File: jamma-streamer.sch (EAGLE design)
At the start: 63 parts, among them IC1 LM7805, J1 Audio line out, J2 ICSP, J3 SDCARD, J4 USB, T1 TY-145P, T2 TY-145P, U1 CD74HC165MD16-M, U10 LM358DTD8-M, U2 ATMEGA328PB-AUR, U3 74HC4050D, U4 TLV757X / LP298X, U5 CD74HC165MD16-M, U6 CD74HC165MD16-M, U7 FT232RL, U8 DS3231SNT&R21-0042B_16-M, U9 NDT2955SOT-223-M, Y1 16MHz

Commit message: Better routing, elec fixes, doc and sdcard ok
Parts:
- added C14: 0.1uF/16V, CMS:KEMET-C1210C104K4J
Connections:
- net GND: now also C14.P$2, J3.DAT1, J3.DAT2
- net VCC: now also C14.P$1
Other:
- note added: "After tests: - DAT1 and DAT2 could be floating or GND - DI = MOSI = CMD - DO = MISO - SCK = CLOCK SD Status is working and inspired from the following: https://learn.adafruit.com/adafruit-micro-sd-breakout-board-card-tutorial?view=all"
- note added: "CS = PB2 (atmega) = Pin 10 (arduino pin number) Used by "ArduinoISP sketch" to send a reset signal when using this ATmega as ISP programmer."
- note removed: "CS = PB2 = Pin 10 Used by ArduinoISP sketch to send a reset signal when using this atmega as ISP programmer"
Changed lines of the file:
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@@
 <part name="GND33" library="SparkFun-PowerSymbols" library_urn="urn:adsk.eagle:library:530" deviceset="GND" device=""/>
 <part name="SUPPLY22" library="SparkFun-PowerSymbols" library_urn="urn:adsk.eagle:library:530" deviceset="VCC" device=""/>
-<part name="SUPPLY23" library="SparkFun-PowerSymbols" library_urn="urn:adsk.eagle:library:530" deviceset="VCCIO" device=""/>
+<part name="C14" library="CMS" deviceset="KEMET-C1210C104K4J" device="" value="0.1uF/16V"/>
+<part name="GND34" library="SparkFun-PowerSymbols" library_urn="urn:adsk.eagle:library:530" deviceset="GND" device=""/>
+<part name="SUPPLY16" library="SparkFun-PowerSymbols" library_urn="urn:adsk.eagle:library:530" deviceset="VCC" device=""/>
 </parts>
 <sheets>
@@
 </segment>
 </net>
-<net name="USBVCC" class="0">
-<segment>
-<pinref part="U9" gate="A" pin="D"/>
-<wire x1="101.6" y1="109.22" x2="109.22" y2="109.22" width="0.1524" layer="91"/>
-<label x="109.22" y="109.22" size="1.27" layer="95" xref="yes"/>
-</segment>
-</net>
 <net name="N$23" class="0">
 <segment>
@@
 </segment>
 </net>
+<net name="USBVCC" class="0">
+<segment>
+<pinref part="U9" gate="A" pin="D"/>
+<wire x1="101.6" y1="109.22" x2="111.76" y2="109.22" width="0.1524" layer="91"/>
+<label x="111.76" y="109.22" size="1.27" layer="95" xref="yes"/>
+</segment>
+</net>
 </nets>
 </sheet>
@@
 <description>Micro SD CARD related circuitry</description>
 <plain>
+<text x="-5.08" y="50.8" size="1.27" layer="91" font="fixed">After tests:
+  - DAT1 and DAT2 could be floating or GND
+  - DI  = MOSI = CMD
+  - DO  = MISO
+  - SCK = CLOCK
+SD Status is working and inspired from the following:
+https://learn.adafruit.com/adafruit-micro-sd-breakout-board-card-tutorial?view=all</text>
 </plain>
 <instances>
@@
 <wire x1="96.52" y1="10.16" x2="96.52" y2="7.62" width="0.1524" layer="91"/>
 <junction x="96.52" y="7.62"/>
+<pinref part="J3" gate="G$1" pin="DAT2"/>
+<wire x1="101.6" y1="17.78" x2="96.52" y2="17.78" width="0.1524" layer="91"/>
+<wire x1="96.52" y1="17.78" x2="96.52" y2="10.16" width="0.1524" layer="91"/>
+<junction x="96.52" y="10.16"/>
+<pinref part="J3" gate="G$1" pin="DAT1"/>
+<wire x1="101.6" y1="20.32" x2="96.52" y2="20.32" width="0.1524" layer="91"/>
+<wire x1="96.52" y1="20.32" x2="96.52" y2="17.78" width="0.1524" layer="91"/>
+<junction x="96.52" y="17.78"/>
 </segment>
 <segment>
@@
 <attribute name="VALUE" x="111.76" y="109.474" size="1.778" layer="96" align="bottom-center"/>
 </instance>
-<instance part="GND6" gate="1" x="111.76" y="45.72" smashed="yes">
-<attribute name="VALUE" x="111.76" y="45.466" size="1.778" layer="96" align="top-center"/>
+<instance part="GND6" gate="1" x="111.76" y="50.8" smashed="yes" rot="R90">
+<attribute name="VALUE" x="112.014" y="50.8" size="1.778" layer="96" rot="R90" align="top-center"/>
 </instance>
 <instance part="R2" gate="A" x="45.72" y="50.8" smashed="yes">
@@
 <instance part="GND15" gate="1" x="27.94" y="93.98" smashed="yes">
 <attribute name="VALUE" x="27.94" y="93.726" size="1.778" layer="96" align="top-center"/>
+</instance>
+<instance part="C14" gate="A" x="119.38" y="101.6" smashed="yes" rot="R90">
+<attribute name="NAME" x="117.88" y="98.6" size="1.27" layer="94" rot="R90"/>
+<attribute name="VALUE" x="122.38" y="98.6" size="1.27" layer="94" rot="R90"/>
+</instance>
+<instance part="GND34" gate="1" x="119.38" y="93.98" smashed="yes">
+<attribute name="VALUE" x="119.38" y="93.726" size="1.778" layer="96" align="top-center"/>
+</instance>
+<instance part="SUPPLY16" gate="G$1" x="119.38" y="106.68" smashed="yes">
+<attribute name="VALUE" x="119.38" y="109.474" size="1.778" layer="96" align="bottom-center"/>
 </instance>
 </instances>
@@
 <segment>
 <pinref part="U2" gate="G$1" pin="GND"/>
-<wire x1="91.44" y1="50.8" x2="111.76" y2="50.8" width="0.1524" layer="91"/>
+<wire x1="91.44" y1="50.8" x2="109.22" y2="50.8" width="0.1524" layer="91"/>
 <pinref part="GND6" gate="1" pin="GND"/>
-<wire x1="111.76" y1="50.8" x2="111.76" y2="48.26" width="0.1524" layer="91"/>
 </segment>
 <segment>
@@
 <wire x1="27.94" y1="97.79" x2="24.13" y2="97.79" width="0.1524" layer="91"/>
 </segment>
+<segment>
+<pinref part="C14" gate="A" pin="P$2"/>
+<wire x1="119.38" y1="98.608" x2="119.38" y2="96.52" width="0.1524" layer="91"/>
+<pinref part="GND34" gate="1" pin="GND"/>
+</segment>
 </net>
 <net name="VCC" class="0">
@@
 <wire x1="24.13" y1="102.87" x2="26.67" y2="102.87" width="0.1524" layer="91"/>
 <label x="26.67" y="102.87" size="1.27" layer="95" font="vector" xref="yes"/>
+</segment>
+<segment>
+<pinref part="C14" gate="A" pin="P$1"/>
+<wire x1="119.38" y1="104.592" x2="119.38" y2="106.68" width="0.1524" layer="91"/>
+<pinref part="SUPPLY16" gate="G$1" pin="VCC"/>
 </segment>
 </net>
@@
 <description>USB input</description>
 <plain>
-<text x="104.14" y="73.66" size="1.778" layer="91">CS = PB2 = Pin 10
-Used by ArduinoISP sketch to send a reset
-signal when using this atmega as ISP programmer</text>
+<text x="104.14" y="73.66" size="1.778" layer="91">CS = PB2 (atmega) = Pin 10 (arduino pin number)
+Used by "ArduinoISP sketch" to send a reset
+signal when using this ATmega as ISP programmer.</text>
 </plain>
 <instances>
@@
 <attribute name="NAME" x="124.46" y="53.34" size="1.778" layer="95"/>
 <attribute name="VALUE" x="124.46" y="46.99" size="1.778" layer="96"/>
-</instance>
-<instance part="SUPPLY23" gate="G$1" x="15.24" y="12.7" smashed="yes" rot="R90">
-<attribute name="VALUE" x="12.446" y="12.7" size="1.778" layer="96" rot="R90" align="bottom-center"/>
 </instance>
 </instances>
@@
 <wire x1="66.04" y1="55.88" x2="66.04" y2="50.8" width="0.1524" layer="91"/>
 <wire x1="66.04" y1="50.8" x2="43.18" y2="50.8" width="0.1524" layer="91"/>
-<wire x1="43.18" y1="50.8" x2="43.18" y2="66.04" width="0.1524" layer="91"/>
 <junction x="43.18" y="50.8"/>
-<label x="43.18" y="66.04" size="1.27" layer="95" rot="R90" xref="yes"/>
+<label x="43.18" y="73.66" size="1.27" layer="95" rot="R90" xref="yes"/>
 <wire x1="68.58" y1="48.26" x2="43.18" y2="48.26" width="0.1524" layer="91"/>
 <junction x="43.18" y="48.26"/>
-</segment>
-<segment>
+<wire x1="43.18" y1="50.8" x2="43.18" y2="73.66" width="0.1524" layer="91"/>
+<wire x1="43.18" y1="72.12" x2="43.18" y2="50.8" width="0.1524" layer="91"/>
+</segment>
+<segment>

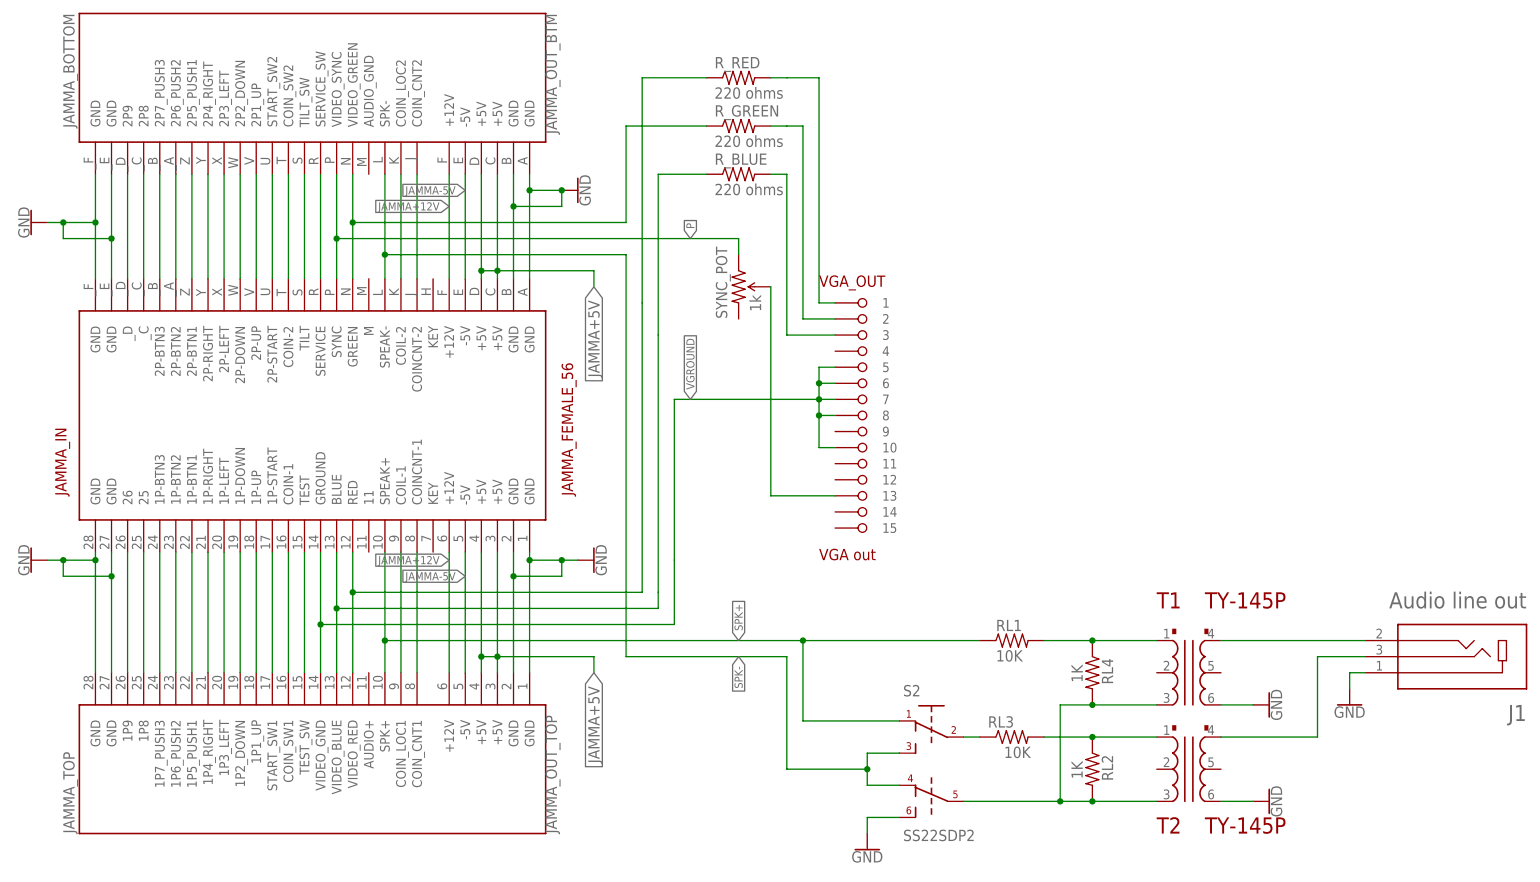
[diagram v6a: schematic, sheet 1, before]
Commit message: Refacto some parts on the PCB
- new SDCARD slot (push-push): https://www.mouser.fr/ProductDetail/798-DM3AT-SF-PEJM5
- new microUSB connector (type B): https://www.mouser.fr/ProductDetail/806-KMMXBSMT35SB30TR
- resistors replacement for audio (3W) -> need to replace with other
values
- resistors replacement for RGB (SMT)
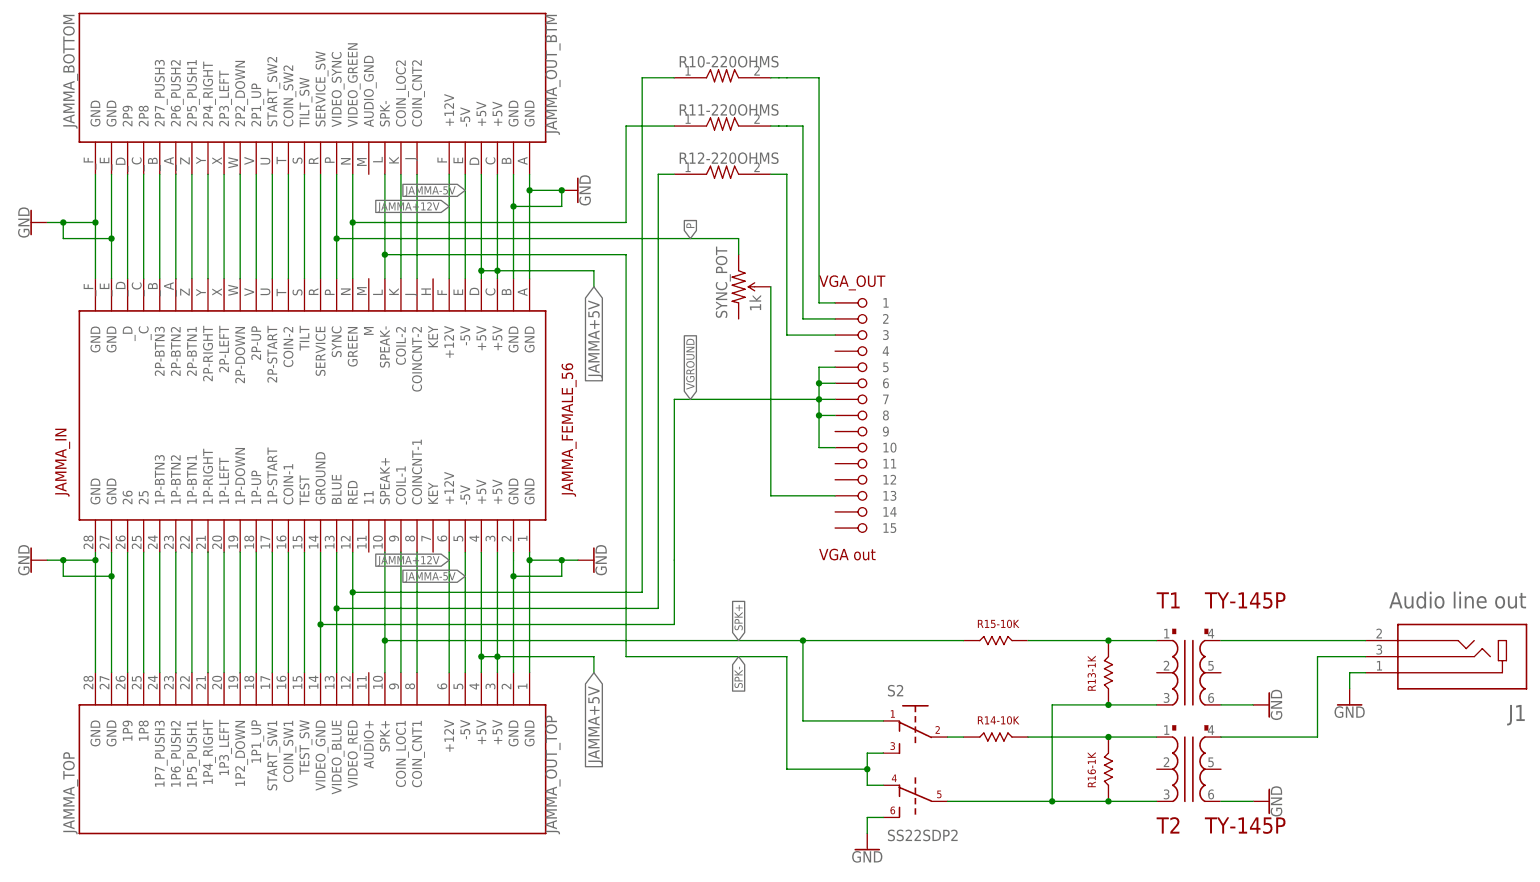
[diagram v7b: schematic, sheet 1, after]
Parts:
- removed J3: SDCARD, DM3CS-SF:DM3CS-SF
- removed RL1, RL3: 10K, rcl:R-US_0204/5
- removed RL2, RL4: 1K, rcl:R-US_0204/5
- removed R_BLUE, R_GREEN, R_RED: 220 ohms, rcl:R-US_0204/5
- added J5: KMMX-BSMT35S-B30TR, KMMX-BSMT35S-B30TR:KMMX-BSMT35S-B30TR
- added R10-220OHMS, R11-220OHMS, R12-220OHMS: CR2512-JW-221ELF, CR2512-JW-221ELF:CR2512-JW-221ELF
- added R13-1K, R16-1K: BOURNS-652CHP0603FX1001ELF, CMS:BOURNS-652CHP0603FX1001ELF
- added R14-10K, R15-10K: BOURNS-CRM2512AJW103ELF, CMS:BOURNS-CRM2512AJW103ELF
- J4: value USB -> DM3AT-SF-PEJM5; device 292304-1:292304-1 -> DM3AT-SF-PEJM5:DM3AT-SF-PEJM5
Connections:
- removed net N$24: RL1.2, RL4.1, T1.1
- removed net N$28: RL2.1, RL3.2, T2.1
- removed net N$5: J4.D+, U7.USBDP
- removed net N$6: J4.D-, U7.USBDM
- removed net N$7: F1.P$1, J4.VBUS
- new net D+: J5.3, U7.USBDP
- new net D-: J5.2, U7.USBDM
- new net N$11: R13-1K.P$2, R15-10K.P$2, T1.1
- new net N$14: R14-10K.P$2, R16-1K.P$2, T2.1
- new net USB_V: F1.P$1, J5.1
- net BLUE: now also R12-220OHMS.1; no longer R_BLUE.1
- net DO: now also J4.DAT0; no longer J3.DAT0
- net GND: now also J4.DAT1, J4.DAT2, J4.VSS, J5.5, J5.MH1, J5.MH2, J5.MH3, J5.MH4; no longer J3.DAT1, J3.DAT2, J3.GND, J3.VSS, J4.GND
- net GREEN: now also R11-220OHMS.1; no longer R_GREEN.1
- net N$1: now also R10-220OHMS.2; no longer R_RED.2
- net N$16: now also R12-220OHMS.2; no longer R_BLUE.2
- net N$2: now also R11-220OHMS.2; no longer R_GREEN.2
- net N$25: now also R13-1K.P$1, R16-1K.P$1; no longer RL2.2, RL4.2
- net N$4: now also R14-10K.P$1; no longer RL3.1
- net RED: now also R10-220OHMS.1; no longer R_RED.1
- net SD_CLK: now also J4.CLK; no longer J3.CLK
- net SD_CMD: now also J4.CMD; no longer J3.CMD
- net SD_CS: now also J4.CD/DAT3; no longer J3.CD/DAT3
- net SPK+: now also R15-10K.P$1; no longer RL1.1
- net VCC_2: now also J4.VDD; no longer J3.VDD
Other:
- moved on the sheet: S2

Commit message: Better resistors for video and audio
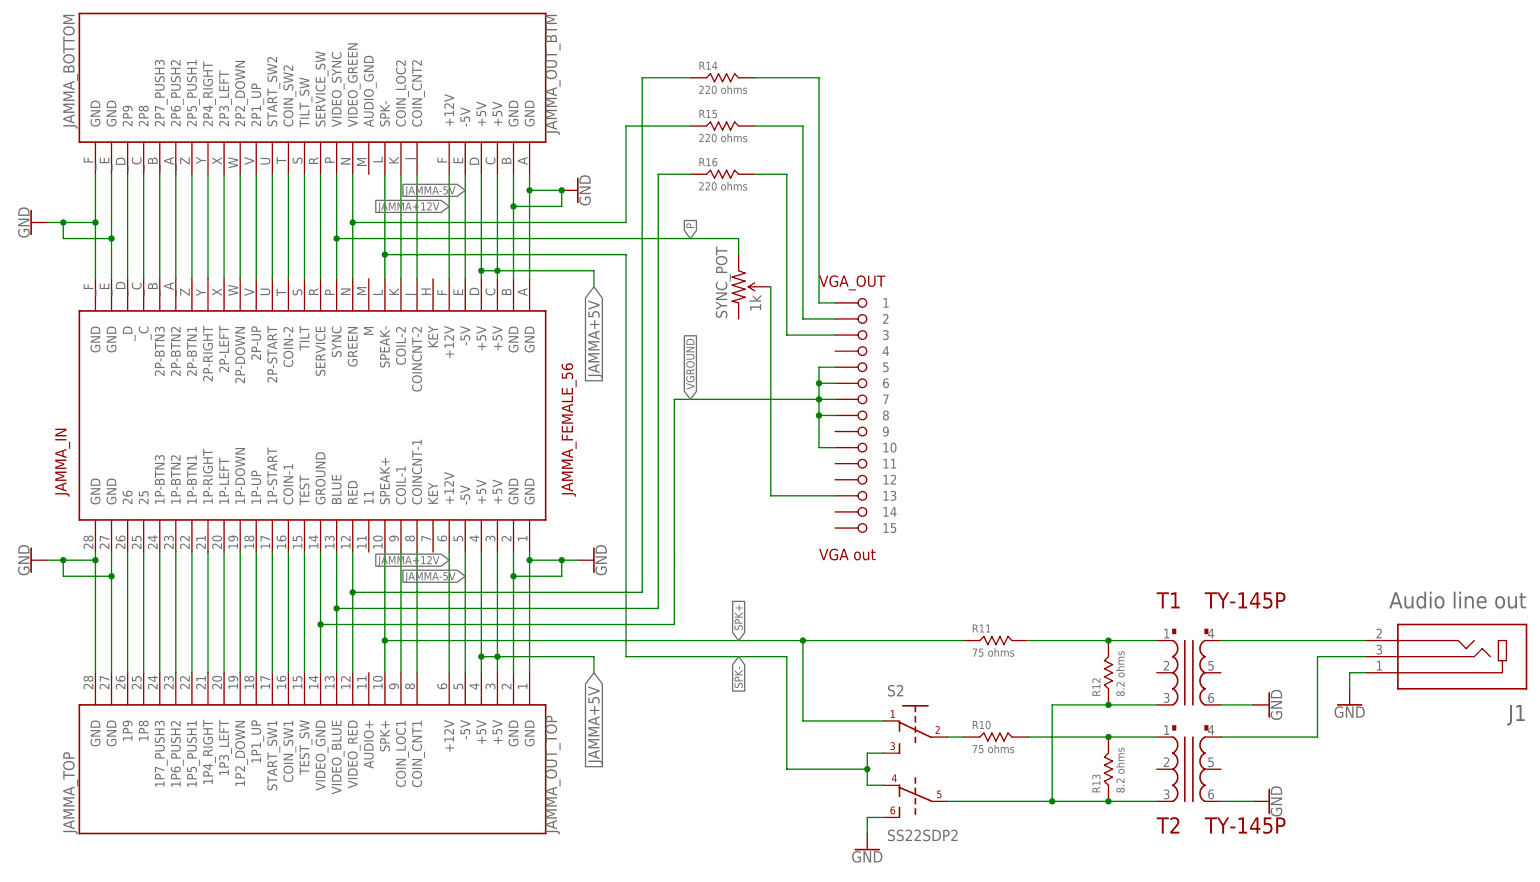
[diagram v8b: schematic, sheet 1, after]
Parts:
- removed R10-220OHMS, R11-220OHMS, R12-220OHMS: CR2512-JW-221ELF, CR2512-JW-221ELF:CR2512-JW-221ELF
- removed R13-1K, R16-1K: BOURNS-652CHP0603FX1001ELF, CMS:BOURNS-652CHP0603FX1001ELF
- removed R14-10K, R15-10K: BOURNS-CRM2512AJW103ELF, CMS:BOURNS-CRM2512AJW103ELF
- added R10, R11: 75 ohms, nma-mouser:TE3550
- added R12, R13: 8.2 ohms, nma-mouser:TE3550
- added R14, R15, R16: 220 ohms, nma-mouser:ERJ-14NF2200U
- J1: SPICEPREFIX (none) -> J
- S2, T1, T2: SPICEPREFIX (none) -> X
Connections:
- net BLUE: now also R16.P$1; no longer R12-220OHMS.1
- net GREEN: now also R15.P$1; no longer R11-220OHMS.1
- net N$1: now also R14.P$2; no longer R10-220OHMS.2
- net N$11: now also R11.P$2, R12.P$2; no longer R13-1K.P$2, R15-10K.P$2
- net N$14: now also R10.P$2, R13.P$2; no longer R14-10K.P$2, R16-1K.P$2
- net N$16: now also R16.P$2; no longer R12-220OHMS.2
- net N$2: now also R15.P$2; no longer R11-220OHMS.2
- net N$25: now also R12.P$1, R13.P$1; no longer R13-1K.P$1, R16-1K.P$1
- net N$4: now also R10.P$1; no longer R14-10K.P$1
- net RED: now also R14.P$1; no longer R10-220OHMS.1
- net SPK+: now also R11.P$1; no longer R15-10K.P$1
